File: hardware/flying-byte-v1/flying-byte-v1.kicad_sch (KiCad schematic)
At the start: 26 parts, among them J1 Conn_Coaxial, J2 Conn_ARM_SWD_TagConnect_TC2030, U1 STM32WB55CEU6, X1 32MHz, X2 32kHz768

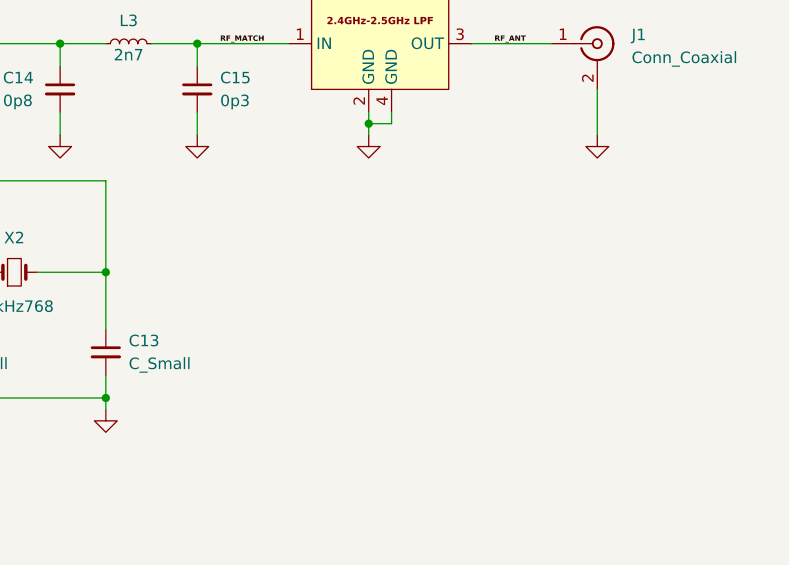
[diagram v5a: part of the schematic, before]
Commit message: feature: Add the BOOT0 interface
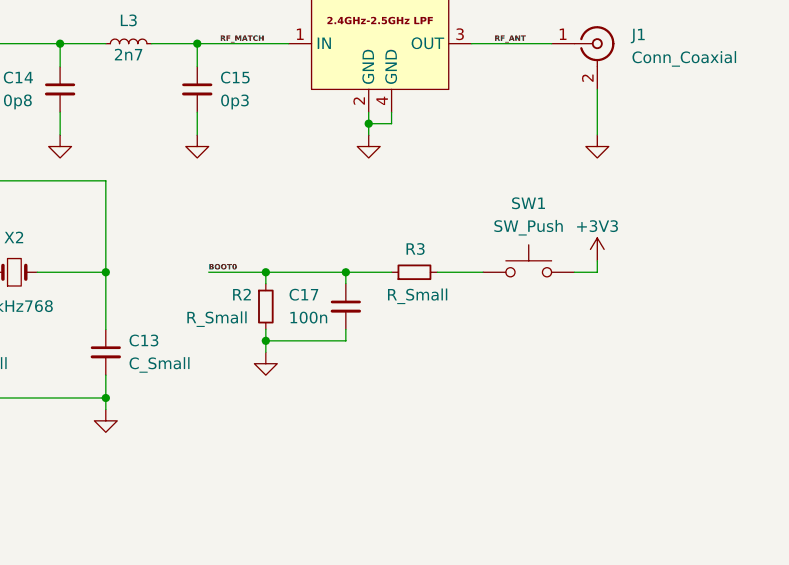
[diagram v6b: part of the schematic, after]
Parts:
- added C17: 100n, symbol Device:C_Small
- added R2, R3: R_Small, symbol Device:R_Small
- added SW1: SW_Push, symbol Switch:SW_Push
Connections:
- net +3V3: now also SW1.2
- net BOOT0: now also C17.1, R2.1, R3.1
- net GND: now also C17.2, R2.2
- new net: R3.2, SW1.1
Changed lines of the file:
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@@
   (junction (at 166.37 57.15) (diameter 0) (color 0 0 0 0)
   )
+  (junction (at 223.52 119.38) (diameter 0) (color 0 0 0 0)
+  )
+  (junction (at 232.41 111.76) (diameter 0) (color 0 0 0 0)
+  )
   (junction (at 120.65 43.18) (diameter 0) (color 0 0 0 0)
   )
@@
   (junction (at 130.81 43.18) (diameter 0) (color 0 0 0 0)
   )
+  (junction (at 223.52 111.76) (diameter 0) (color 0 0 0 0)
+  )
   (junction (at 130.81 29.21) (diameter 0) (color 0 0 0 0)
   )
@@
     (stroke (width 0) (type default))
   )
+  (wire (pts (xy 232.41 113.03) (xy 232.41 111.76))
+    (stroke (width 0) (type default))
+  )
   (wire (pts (xy 185.42 110.49) (xy 185.42 111.76))
     (stroke (width 0) (type default))
@@
     (stroke (width 0) (type default))
   )
+  (wire (pts (xy 232.41 111.76) (xy 237.49 111.76))
+    (stroke (width 0) (type default))
+  )
   (wire (pts (xy 156.21 138.43) (xy 156.21 139.7))
     (stroke (width 0) (type default))
@@
     (stroke (width 0) (type default))
   )
+  (wire (pts (xy 223.52 111.76) (xy 223.52 113.03))
+    (stroke (width 0) (type default))
+  )
   (wire (pts (xy 191.77 68.58) (xy 196.85 68.58))
     (stroke (width 0) (type default))
   )
+  (wire (pts (xy 260.35 110.49) (xy 260.35 111.76))
+    (stroke (width 0) (type default))
+  )
   (wire (pts (xy 199.39 74.93) (xy 199.39 77.47))
     (stroke (width 0) (type default))
@@
     (stroke (width 0) (type default))
   )
+  (wire (pts (xy 257.81 111.76) (xy 260.35 111.76))
+    (stroke (width 0) (type default))
+  )
   (wire (pts (xy 90.17 50.8) (xy 81.28 50.8))
     (stroke (width 0) (type default))
@@
     (stroke (width 0) (type default))
   )
+  (wire (pts (xy 223.52 119.38) (xy 232.41 119.38))
+    (stroke (width 0) (type default))
+  )
+  (wire (pts (xy 217.17 111.76) (xy 223.52 111.76))
+    (stroke (width 0) (type default))
+  )
   (wire (pts (xy 110.49 49.53) (xy 110.49 50.8))
     (stroke (width 0) (type default))
@@
     (stroke (width 0) (type default))
   )
+  (wire (pts (xy 223.52 111.76) (xy 232.41 111.76))
+    (stroke (width 0) (type default))
+  )
   (wire (pts (xy 209.55 71.12) (xy 209.55 68.58))
     (stroke (width 0) (type default))
@@
     (stroke (width 0) (type default))
   )
+  (wire (pts (xy 223.52 118.11) (xy 223.52 119.38))
+    (stroke (width 0) (type default))
+  )
   (wire (pts (xy 158.75 137.16) (xy 158.75 138.43))
     (stroke (width 0) (type default))
@@
     (stroke (width 0) (type default))
   )
+  (wire (pts (xy 223.52 119.38) (xy 223.52 120.65))
+    (stroke (width 0) (type default))
+  )
   (wire (pts (xy 130.81 49.53) (xy 130.81 50.8))
     (stroke (width 0) (type default))
@@
     (stroke (width 0) (type default))
   )
+  (wire (pts (xy 242.57 111.76) (xy 247.65 111.76))
+    (stroke (width 0) (type default))
+  )
   (wire (pts (xy 140.97 35.56) (xy 140.97 36.83))
     (stroke (width 0) (type default))
@@
     (stroke (width 0) (type default))
   )
+  (wire (pts (xy 232.41 118.11) (xy 232.41 119.38))
+    (stroke (width 0) (type default))
+  )
   (wire (pts (xy 90.17 49.53) (xy 90.17 50.8))
     (stroke (width 0) (type default))
@@
   (wire (pts (xy 128.27 96.52) (xy 138.43 96.52))
     (stroke (width 0) (type default))
+  )
+  (label "BOOT0" (at 217.17 111.76 0) (fields_autoplaced)
+    (effects (font (size 0.6 0.6) (thickness 0.21) bold) (justify left bottom))
   )
   (label "SWD_DIO" (at 133.35 96.52 0) (fields_autoplaced)
@@
     )
   )
+  (symbol (lib_id "Device:C_Small") (at 232.41 115.57 0) (unit 1)
+    (in_bom yes) (on_board yes) (dnp no)
+    (property "Reference" "C17" (at 226.06 114.3 0)
+      (effects (font (size 1.27 1.27)) (justify left))
+    )
+    (property "Value" "100n" (at 226.06 116.84 0)
+      (effects (font (size 1.27 1.27)) (justify left))
+    )
+    (property "Footprint" "" (at 232.41 115.57 0)
+      (effects (font (size 1.27 1.27)) hide)
+    )
+    (property "Datasheet" "~" (at 232.41 115.57 0)
+      (effects (font (size 1.27 1.27)) hide)
+    )
+    (pin "1")
+    (pin "2")
+    (instances
+      (project "flying-byte-v1"
+        (path "/89251f6d-2a03-4ee6-93f4-15acd18dfc68"
+          (reference "C17") (unit 1)
+        )
+      )
+    )
+  )
   (symbol (lib_id "Device:C_Small") (at 130.81 33.02 0) (unit 1)
     (in_bom yes) (on_board yes) (dnp no) (fields_autoplaced)
@@
     )
   )
+  (symbol (lib_id "Device:R_Small") (at 223.52 115.57 0) (unit 1)
+    (in_bom yes) (on_board yes) (dnp no)
+    (property "Reference" "R2" (at 219.71 114.3 0)
+      (effects (font (size 1.27 1.27)) (justify left))
+    )
+    (property "Value" "R_Small" (at 214.63 116.84 0)
+      (effects (font (size 1.27 1.27)) (justify left))
+    )
+    (property "Footprint" "" (at 223.52 115.57 0)
+      (effects (font (size 1.27 1.27)) hide)
+    )
+    (property "Datasheet" "~" (at 223.52 115.57 0)
+      (effects (font (size 1.27 1.27)) hide)
+    )
+    (pin "1")
+    (pin "2")
+    (instances
+      (project "flying-byte-v1"
+        (path "/89251f6d-2a03-4ee6-93f4-15acd18dfc68"
+          (reference "R2") (unit 1)
+        )
+      )
+    )
+  )
   (symbol (lib_id "Device:C_Small") (at 209.55 73.66 0) (unit 1)
     (in_bom yes) (on_board yes) (dnp no) (fields_autoplaced)
@@
         (path "/89251f6d-2a03-4ee6-93f4-15acd18dfc68"
           (reference "C11") (unit 1)
+        )
+      )
+    )
+  )
+  (symbol (lib_id "Device:R_Small") (at 240.03 111.76 90) (unit 1)
+    (in_bom yes) (on_board yes) (dnp no)
+    (property "Reference" "R3" (at 241.3 109.22 90)
+      (effects (font (size 1.27 1.27)) (justify left))
+    )
+    (property "Value" "R_Small" (at 243.84 114.3 90)
+      (effects (font (size 1.27 1.27)) (justify left))
+    )
+    (property "Footprint" "" (at 240.03 111.76 0)
+      (effects (font (size 1.27 1.27)) hide)
+    )
+    (property "Datasheet" "~" (at 240.03 111.76 0)
+      (effects (font (size 1.27 1.27)) hide)
+    )
+    (pin "1")
+    (pin "2")
+    (instances
+      (project "flying-byte-v1"
+        (path "/89251f6d-2a03-4ee6-93f4-15acd18dfc68"
+          (reference "R3") (unit 1)
+        )
+      )
+    )
+  )
+  (symbol (lib_id "power:GND") (at 223.52 120.65 0) (unit 1)
+    (in_bom yes) (on_board yes) (dnp no) (fields_autoplaced)
+    (property "Reference" "#PWR018" (at 223.52 127 0)
+      (effects (font (size 1.27 1.27)) hide)
+    )
+    (property "Value" "GND" (at 223.52 125.73 0)
+      (effects (font (size 1.27 1.27)) hide)
+    )
+    (property "Footprint" "" (at 223.52 120.65 0)
+      (effects (font (size 1.27 1.27)) hide)
+    )
+    (property "Datasheet" "" (at 223.52 120.65 0)
+      (effects (font (size 1.27 1.27)) hide)
+    )
+    (pin "1")
+    (instances
+      (project "flying-byte-v1"
+        (path "/89251f6d-2a03-4ee6-93f4-15acd18dfc68"
+          (reference "#PWR018") (unit 1)
         )
       )
@@
     )
   )
+  (symbol (lib_id "power:+3V3") (at 260.35 110.49 0) (unit 1)
+    (in_bom yes) (on_board yes) (dnp no)
+    (property "Reference" "#PWR019" (at 260.35 114.3 0)
+      (effects (font (size 1.27 1.27)) hide)
+    )
+    (property "Value" "+3V3" (at 260.35 106.68 0)
+      (effects (font (size 1.27 1.27)))
+    )
+    (property "Footprint" "" (at 260.35 110.49 0)
+      (effects (font (size 1.27 1.27)) hide)
+    )
+    (property "Datasheet" "" (at 260.35 110.49 0)
+      (effects (font (size 1.27 1.27)) hide)
+    )
+    (pin "1")
+    (instances
+      (project "flying-byte-v1"
+        (path "/89251f6d-2a03-4ee6-93f4-15acd18dfc68"
+          (reference "#PWR019") (unit 1)
+        )
+      )
+    )
+  )
   (symbol (lib_id "power:GND") (at 234.95 96.52 0) (unit 1)
     (in_bom yes) (on_board yes) (dnp no) (fields_autoplaced)
@@
         )
       )
+    )
+  )
+  (symbol (lib_id "Switch:SW_Push") (at 252.73 111.76 0) (unit 1)
+    (in_bom yes) (on_board yes) (dnp no) (fields_autoplaced)
+    (property "Reference" "SW1" (at 252.73 104.14 0)
+      (effects (font (size 1.27 1.27)))
+    )
+    (property "Value" "SW_Push" (at 252.73 106.68 0)
+      (effects (font (size 1.27 1.27)))
+    )
+    (property "Footprint" "" (at 252.73 106.68 0)
+      (effects (font (size 1.27 1.27)) hide)
+    )
+    (property "Datasheet" "~" (at 252.73 106.68 0)
+      (effects (font (size 1.27 1.27)) hide)
+    )
+    (pin "1")
+    (pin "2")
+    (instances
+      (project "flying-byte-v1"
+        (path "/89251f6d-2a03-4ee6-93f4-15acd18dfc68"
+          (reference "SW1") (unit 1)
+        )
+      )

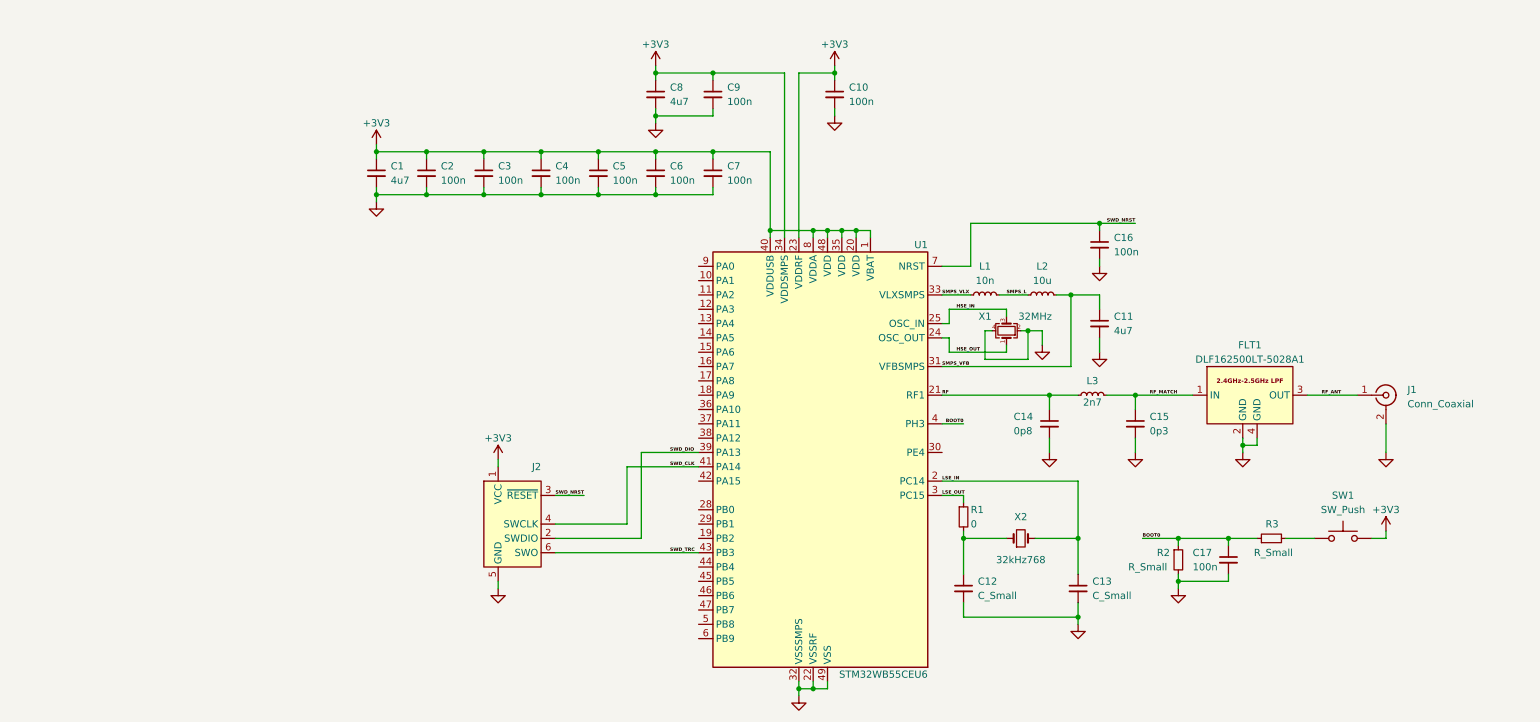
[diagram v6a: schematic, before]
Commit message: feature: Add the USBC and ESD protection
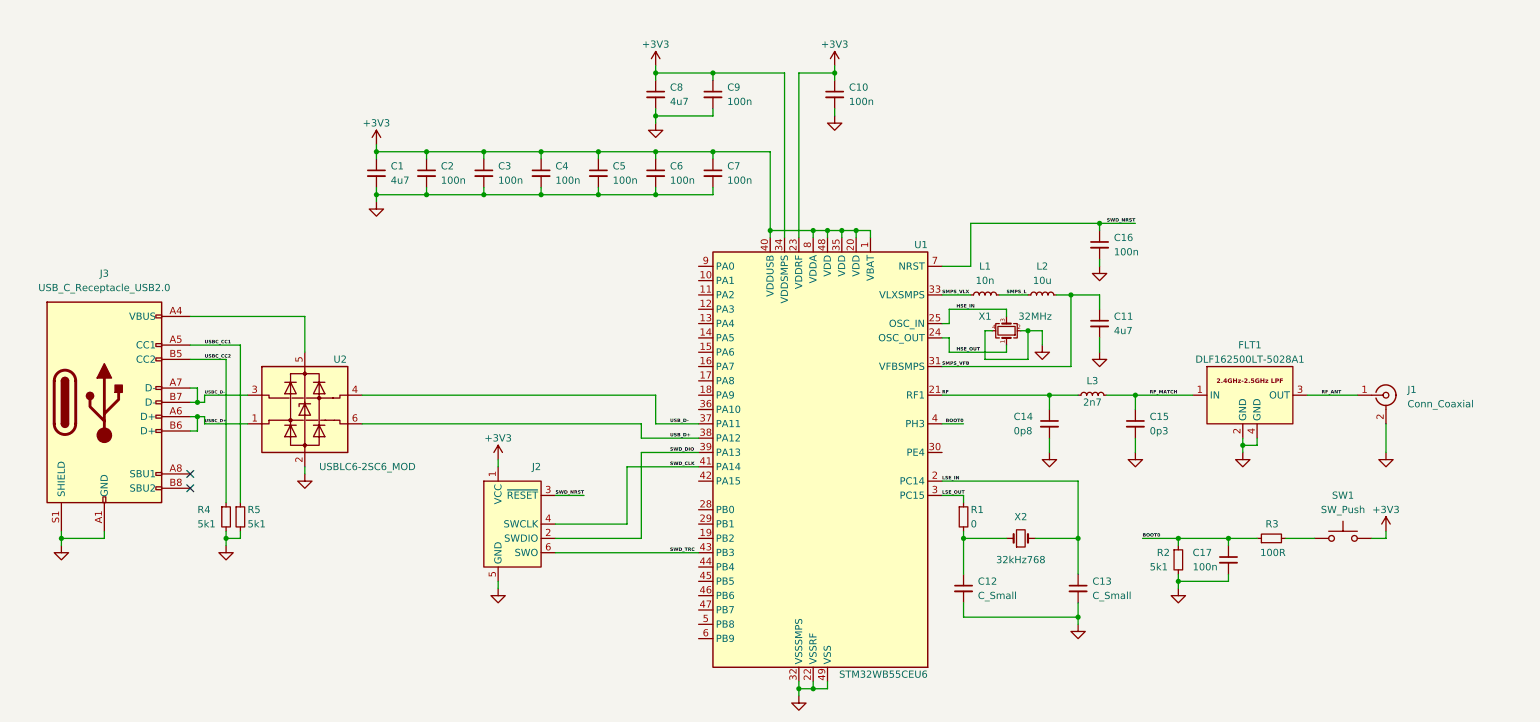
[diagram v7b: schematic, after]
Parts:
- added J3: USB_C_Receptacle_USB2.0, symbol Connector:USB_C_Receptacle_USB2.0
- added R4, R5: 5k1, symbol Device:R_Small
- added U2: USBLC6-2SC6_MOD, Package_TO_SOT_SMD:SOT-23-6, symbol Power_Protection:USBLC6-2SC6_MOD
- R2: value R_Small -> 5k1
- R3: value R_Small -> 100R
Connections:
- net GND: now also J3.A1 (GND), J3.A12 (GND), J3.B1 (GND), J3.B12 (GND), J3.S1 (SHIELD), R4.2, R5.2, U2.2 (GND)
- net USB_D-: now reaches U1.37 (PA11)
- net USB_D-: now also U2.4 (I/O2)
- net USB_D+: now reaches U1.38 (PA12)
- net USB_D+: now also U2.6 (I/O2)
- new net: J3.A4 (VBUS), J3.A9 (VBUS), J3.B4 (VBUS), J3.B9 (VBUS), U2.5 (VBUS)
- new net USBC_CC1: J3.A5 (CC1), R5.1
- new net USBC_CC2: J3.B5 (CC2), R4.1
- new net USBC_D+: J3.A6 (D+), J3.B6 (D+), U2.1 (I/O1)
- new net USBC_D-: J3.A7 (D-), J3.B7 (D-), U2.3 (I/O1)
- no-connect marks 0 -> 2

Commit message: feature: Add the 3V3 LDO regulator, LEDs and UART connector.
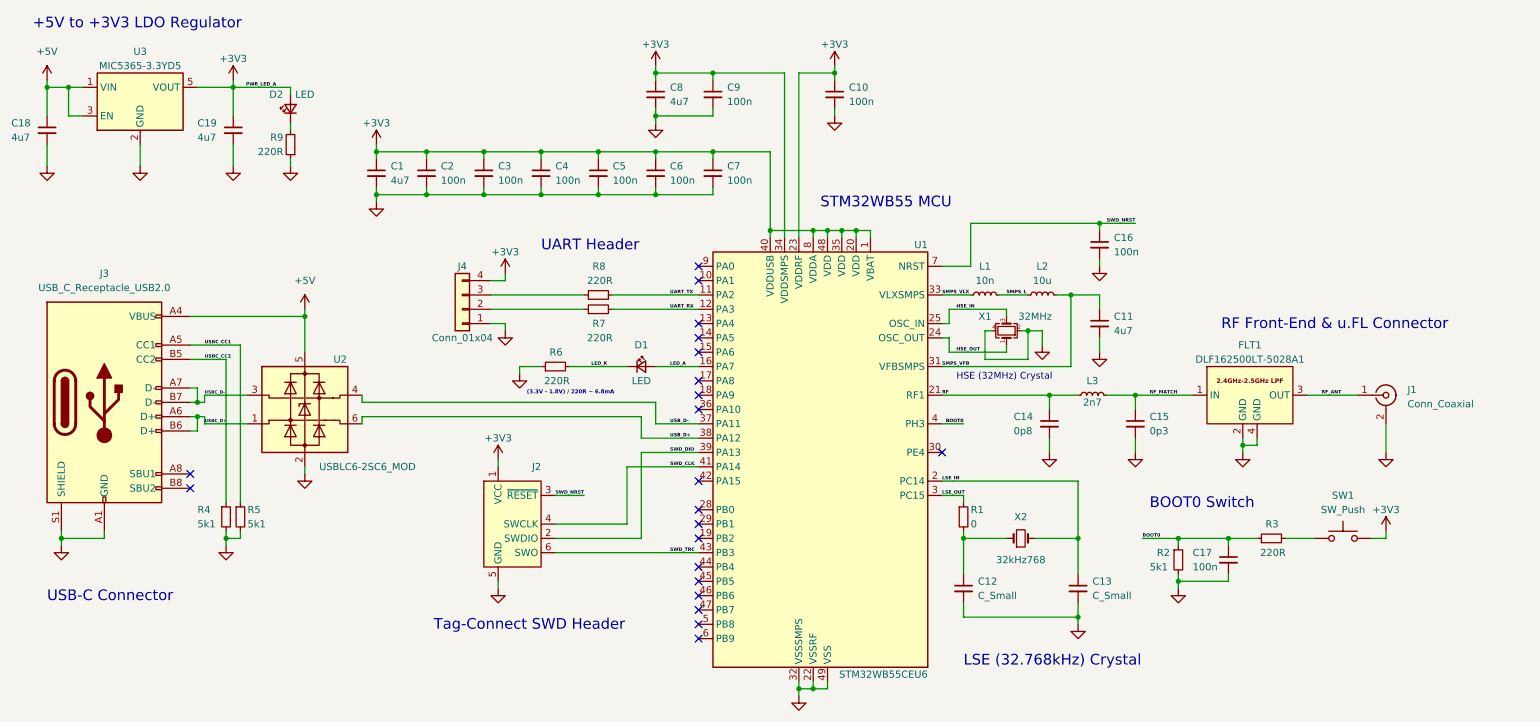
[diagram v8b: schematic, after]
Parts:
- added C18, C19: 4u7, symbol Device:C_Small
- added D1, D2: LED, symbol Device:LED_Small
- added J4: Conn_01x04, symbol Connector_Generic:Conn_01x04
- added R6, R7, R8, R9: 220R, symbol Device:R_Small
- added U3: MIC5365-3.3YD5, Package_TO_SOT_SMD:SOT-23-5, symbol Regulator_Linear:MIC5365-3.3YD5
- R3: value 100R -> 220R
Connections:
- net +3V3: now also C19.1, D2.2 (A), J4.4 (Pin_4), U3.5 (VOUT)
- net GND: now also C18.2, C19.2, J4.1 (Pin_1), R6.1, R9.1, U3.2 (GND)
- net +5V: now reaches J3.A4 (VBUS), J3.A9 (VBUS), J3.B4 (VBUS), J3.B9 (VBUS), U2.5 (VBUS)
- net +5V: now also C18.1, U3.1 (VIN), U3.3 (EN)
- net UART_TX: now reaches U1.11 (PA2)
- net UART_TX: now also R8.2
- net UART_RX: now reaches U1.12 (PA3)
- net UART_RX: now also R7.2
- net LED_A: now reaches U1.16 (PA7)
- net LED_A: now also D1.2 (A)
- new net: D2.1 (K), R9.2
- new net: J4.3 (Pin_3), R8.1
- new net: J4.2 (Pin_2), R7.1
- new net LED_K: D1.1 (K), R6.2
- no-connect marks 2 -> 21
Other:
- note added: "(3.3V - 1.8V) / 220R ~ 6.8mA"
- note added: "+5V to +3V3 LDO Regulator"
- note added: "BOOT0 Switch"
- note added: "HSE (32MHz) Crystal"
- note added: "LSE (32.768kHz) Crystal"
- note added: "RF Front-End & u.FL Connector"
- note added: "STM32WB55 MCU"
- note added: "Tag-Connect SWD Header"
- note added: "UART Header"
- note added: "USB-C Connector"
